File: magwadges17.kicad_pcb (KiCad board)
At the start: 2 copper layers, 156 x 89.8 mm, 58 parts, among them J1 CONN_02X03, J2 JACK_2P, Q1 BC846BDW1, Q2 BC846BDW1, U1 ATTINY2313-20MU, U2 FT25H16

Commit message: Updated schematic
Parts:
- added Gsp: LOGO, custom:spiral_pattern_large4, F.Cu at (150.0, 100.0)
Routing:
- net TouchA: track 22.8 -> 55.8 mm, vias 0 -> 4
- net TouchB: track 25.2 -> 56.7 mm, vias 0 -> 2
- net Net-(Q2-Pad3): track 93.8 -> 97.9 mm
- net Net-(J2-Pad2): track 127.8 -> 128.9 mm

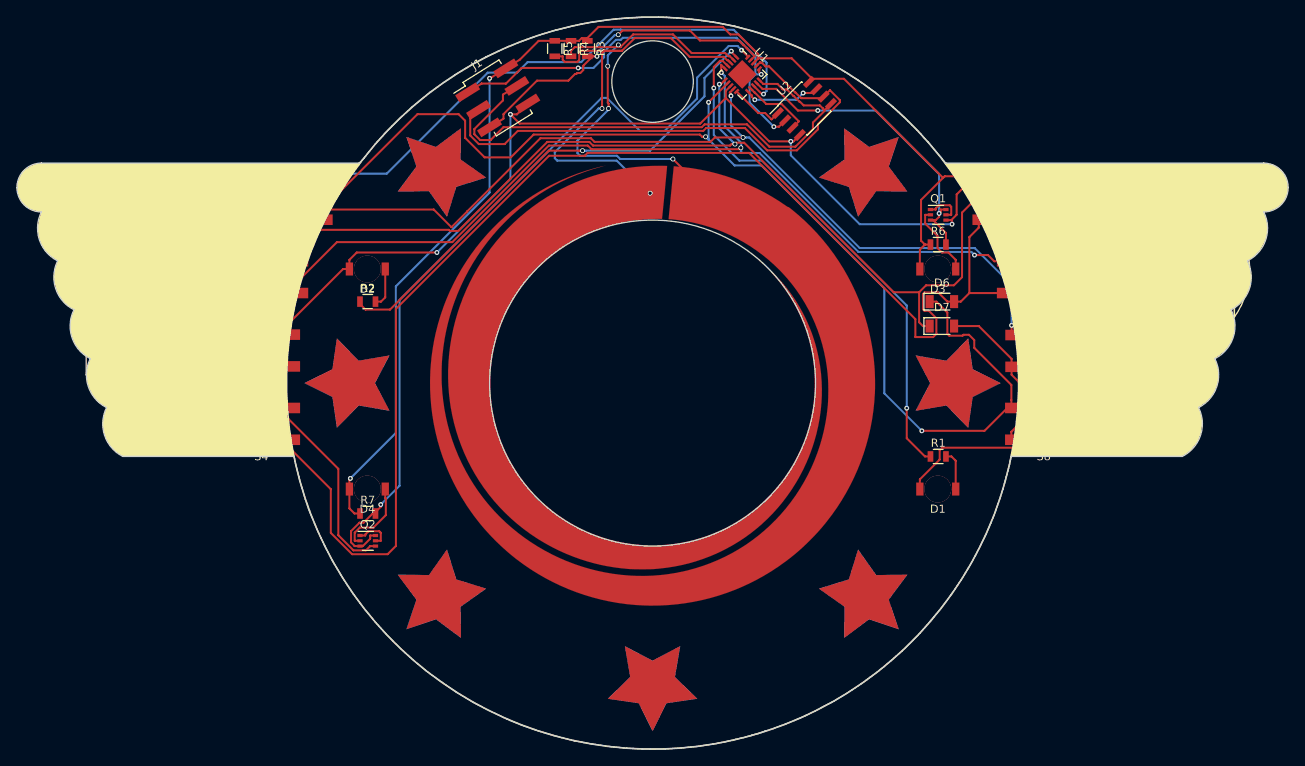
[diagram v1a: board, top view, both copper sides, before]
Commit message: single layer in
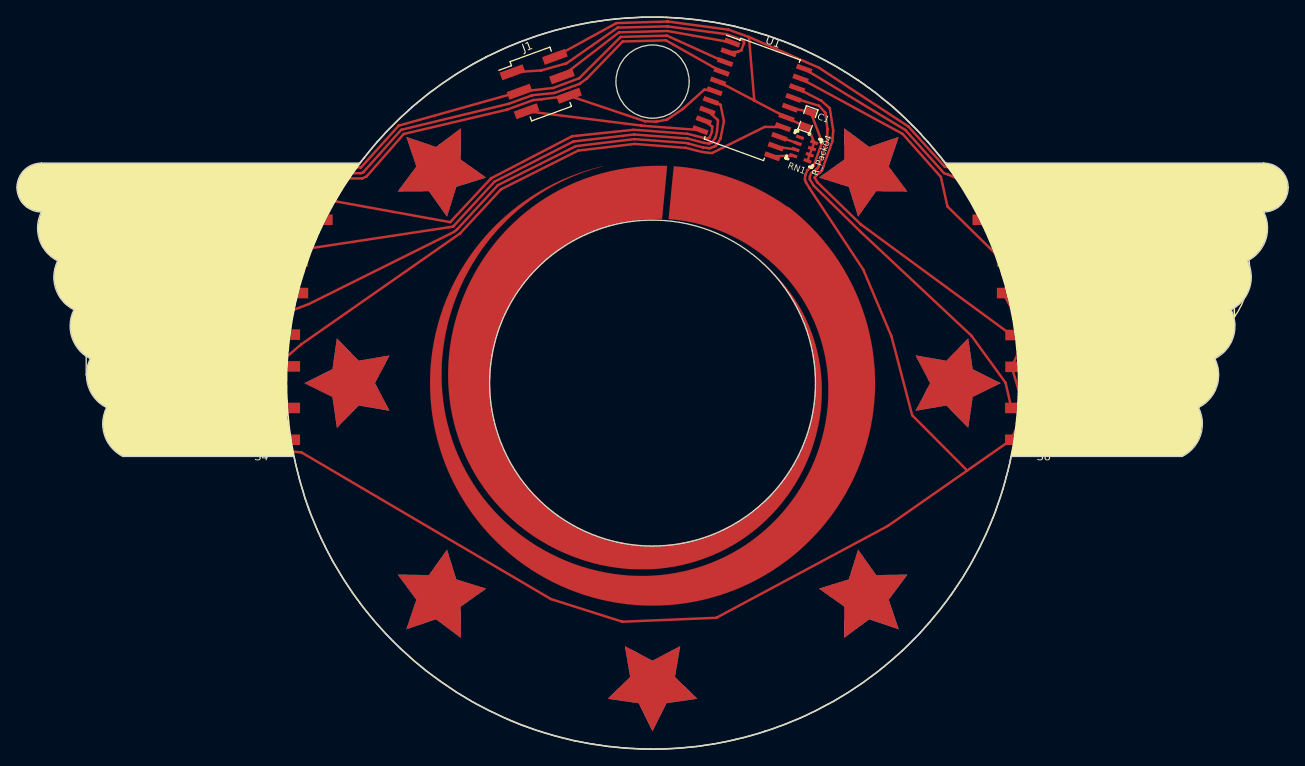
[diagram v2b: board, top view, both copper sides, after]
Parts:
- removed D1, D2, D3, D4: LED, custom:LTST-C230KRKT
- removed D5, D6, D7: D, Diodes_SMD:D_1206
- removed Q1, Q2: BC846BDW1, TO_SOT_Packages_SMD:SOT-363_SC-70-6
- removed R1, R2: 47, Resistors_SMD:R_0805
- removed R3: 1K, Resistors_SMD:R_0805
- removed R4, R5: 1M, Resistors_SMD:R_0805
- removed R6, R7: 2K2, Resistors_SMD:R_0805
- removed U2: FT25H16, Housings_SOIC:SOIC-8_3.9x4.9mm_Pitch1.27mm
- added C1: BYP, SM0805, F.Cu at (169.1, 67.7)
- added RN1: R_Pack04, NETWORK1206, F.Cu at (168.6, 71.3)
- J1: value CONN_02X03 -> PGM
- U1: value ATTINY2313-20MU -> ATTINY861A-SU; footprint Housings_DFN_QFN:QFN-20-1EP_4x4mm_Pitch0.5mm -> Housings_SOIC:SOIC-20W_7.5x12.8mm_Pitch1.27mm
- moved J1 5.55 mm to (136.3, 63.3), turned to 20 degrees
- moved U1 3.31 mm to (162.2, 65.2), turned to 340 degrees
- turned LS1 to 180 degrees
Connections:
- LS1 pad 2: GND -> Net-(J1-Pad3)
- S1 pad 1: Net-(D6-Pad1) -> SW_H
- S1 pad 2: Net-(S1-Pad2) -> (no net)
- S1 pad 3: Net-(D5-Pad2) -> GND
- S1 pad 4: Net-(S1-Pad4) -> (no net)
- S2 pad 1: Net-(D7-Pad1) -> SW_G
- S2 pad 2: Net-(S2-Pad2) -> (no net)
- S2 pad 3: Net-(D5-Pad2) -> GND
- S2 pad 4: Net-(S2-Pad4) -> (no net)
- S3 pad 1: Net-(S3-Pad1) -> SW_F
- S3 pad 2: Net-(S3-Pad2) -> (no net)
- S3 pad 3: Net-(D5-Pad2) -> GND
- S3 pad 4: Net-(S3-Pad4) -> (no net)
- S4 pad 1: Net-(D5-Pad1) -> SW_E
- S4 pad 2: Net-(S4-Pad2) -> (no net)
- S4 pad 3: Net-(D6-Pad2) -> GND
- S4 pad 4: Net-(S4-Pad4) -> (no net)
- S5 pad 1: Net-(D7-Pad1) -> SW_A
- S5 pad 2: Net-(S5-Pad2) -> (no net)
- S5 pad 3: Net-(D6-Pad2) -> GND
- S5 pad 4: Net-(S5-Pad4) -> (no net)
- S6 pad 1: Net-(S3-Pad1) -> SW_B
- S6 pad 2: Net-(S6-Pad2) -> (no net)
- S6 pad 3: Net-(D6-Pad2) -> GND
- S6 pad 4: Net-(S6-Pad4) -> (no net)
- S7 pad 1: Net-(D5-Pad1) -> SW_C
- S7 pad 2: Net-(S7-Pad2) -> (no net)
- S7 pad 3: Net-(D7-Pad2) -> GND
- S7 pad 4: Net-(S7-Pad4) -> (no net)
- S8 pad 1: Net-(D6-Pad1) -> SW_D
- S8 pad 2: Net-(S8-Pad2) -> (no net)
- S8 pad 3: Net-(D7-Pad2) -> GND
- S8 pad 4: Net-(S8-Pad4) -> (no net)
- U1 pad 1: Net-(R2-Pad1) -> Net-(J1-Pad4)
- U1 pad 10: Net-(U1-Pad10) -> reset
- U1 pad 11: Net-(U1-Pad11) -> TouchC
- U1 pad 12: Net-(U1-Pad12) -> TouchB
- U1 pad 13: Net-(J2-Pad2) -> TouchA
- U1 pad 14: Net-(Q1-Pad3) -> SW_E
- U1 pad 15: Net-(J1-Pad4) -> VCC
- U1 pad 16: Net-(J1-Pad1) -> GND
- U1 pad 17: Net-(J1-Pad3) -> SW_D
- U1 pad 18: VCC -> SW_C
- U1 pad 19: reset -> SW_B
- U1 pad 2: TouchA -> Net-(J1-Pad1)
- U1 pad 20: Net-(Q2-Pad3) -> SW_A
- U1 pad 3: TouchB -> Net-(J1-Pad3)
- U1 pad 4: Net-(R1-Pad1) -> Net-(J2-Pad2)
- U1 pad 5: Net-(S3-Pad1) -> VCC
- U1 pad 6: Net-(D7-Pad1) -> GND
- U1 pad 7: Net-(D6-Pad1) -> SW_F
- U1 pad 8: GND -> SW_G
- U1 pad 9: Net-(D5-Pad1) -> SW_H
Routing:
- net Net-(D6-Pad2): track 170.8 -> 0.00 mm
- net Net-(D6-Pad1): track 153.3 -> 0.00 mm, vias 3 -> 0
- net Net-(D5-Pad1): track 150.8 -> 0.00 mm, vias 3 -> 0
- net Net-(D7-Pad1): track 129.9 -> 0.00 mm, vias 2 -> 0
- net Net-(S3-Pad1): track 123.5 -> 0.00 mm, vias 3 -> 0
- net Net-(Q2-Pad3): track 97.9 -> 0.00 mm, vias 2 -> 0
- net SW_E: track 0.00 -> 79.6 mm
- net SW_F: track 0.00 -> 72.9 mm
- net SW_G: track 0.00 -> 67.0 mm
- net VCC: track 193.0 -> 127.7 mm, vias 2 -> 0
- net Net-(R1-Pad1): track 63.1 -> 0.00 mm, vias 2 -> 0
- net SW_H: track 0.00 -> 61.8 mm
- net Net-(R2-Pad1): track 61.6 -> 0.00 mm, vias 2 -> 0
- net TouchB: track 56.7 -> 2.44 mm, vias 2 -> 0
- net TouchA: track 55.8 -> 2.39 mm, vias 4 -> 0
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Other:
- outline, holes or cut-outs redrawn
- net class Default: clearance 0.2 -> 0.254; trace_width 0.25 -> 0.3048
- rule trace_clearance: 0.2 -> 0.254
